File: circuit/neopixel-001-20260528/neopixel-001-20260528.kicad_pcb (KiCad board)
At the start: 2 copper layers, 114.3 x 114.3 mm, 67 parts, among them J1 Conn_NeoPixel, J2 Conn_01x02_Pin, J3 Conn_01x02_Pin, P1 ESP32C3_{1}, P10 unitV3, P11 unitV4, P12 unitV4, P2 ESP32C3_{1}, P3 ESP32C3_{2}, P4 ESP32C3_{2}, P5 unitV1, P6 unitV1, P7 unitV2, P8 unitV2, P9 unitV3, SW1 SW_SPST_LED, SW2 SW_SPST_LED, SW3 SW_SPST_LED, SW4 SW_SPST_LED, U1 SSD1306, U2 Aexit_0-50_Voltmeter

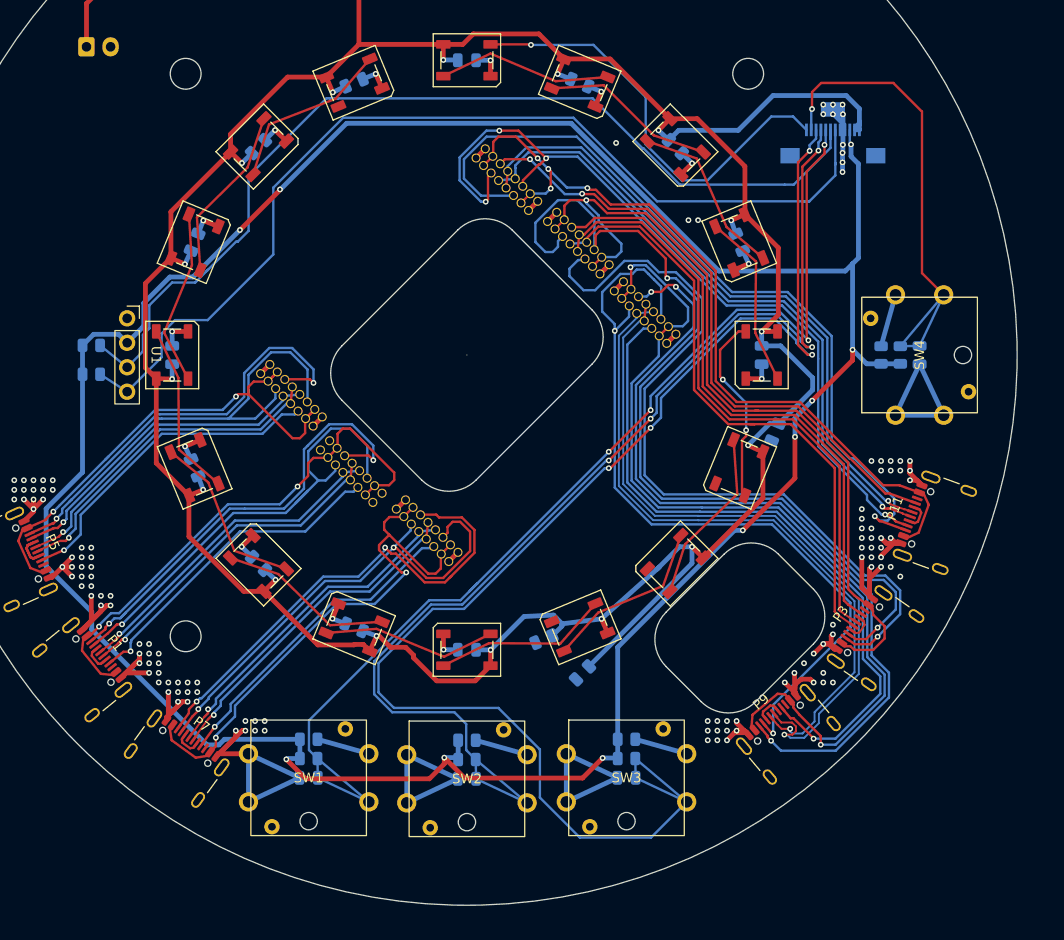
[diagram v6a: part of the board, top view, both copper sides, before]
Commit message: Update ネオピクセル基板のPCBを進めた。タクトスイッチだけ怪しい
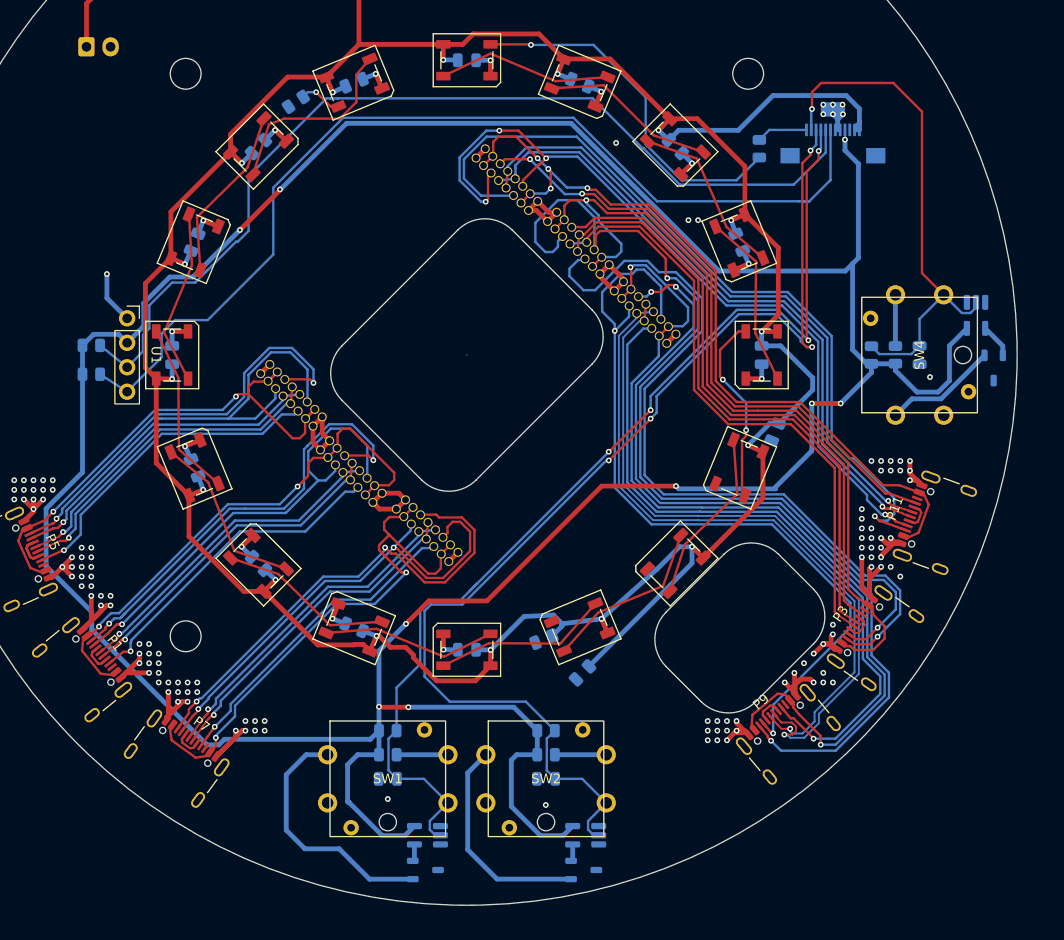
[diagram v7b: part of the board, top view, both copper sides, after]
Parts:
- removed C20: 100n, Capacitor_SMD:C_0805_2012Metric
- removed SW3: SW_SPST_LED, @Thrive_footprint_neopixel:ST-12-401FC-G
- added Q1: NMOS, Package_TO_SOT_SMD:TSOT-23, B.Cu at (-4.31, 53.5)
- added Q2: NMOS, Package_TO_SOT_SMD:TSOT-23, B.Cu at (12.1, 53.5)
- added Q3: NMOS, Package_TO_SOT_SMD:TSOT-23, B.Cu at (54.7, 1.34)
- added U3: 74AHC1G04, Package_TO_SOT_SMD:SOT-23-5_HandSoldering, B.Cu at (-4.10, 49.9)
- added U4: 74AHC1G04, Package_TO_SOT_SMD:SOT-23-5_HandSoldering, B.Cu at (12.3, 49.9)
- added U5: 74AHC1G04, Package_TO_SOT_SMD:SOT-23-5_HandSoldering, B.Cu at (52.9, -4.12)
- R10: value 330 -> 500
- R9: value 10k -> 500
- moved R10 66.2 mm to (-17.8, -26.3), turned to -146.25 degrees
- moved C19 53.4 mm to (47.0, 0.00), turned to 90 degrees
- moved R7 49.0 mm to (42.0, 0.00), turned to -90 degrees
- moved R8 48.7 mm to (44.5, -0.02), turned to -90 degrees
- moved R9 25.9 mm to (30.4, -21.4)
- moved R5 8.75 mm to (8.22, 39.0)
- moved R3 8.71 mm to (-8.22, 39.0)
- moved R4 8.37 mm to (-8.22, 41.5)
- moved R6 8.35 mm to (8.22, 41.5)
- moved C17 8.22 mm to (-8.22, 44.0)
- moved SW1 8.22 mm to (-8.22, 44.0)
- moved C18 8.22 mm to (8.22, 44.0)
- moved SW2 8.22 mm to (8.22, 44.0)
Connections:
- C19 pad 2: SW_{TCT3} -> SW_{START}
- D1 pad 4: SIG_{NeoPixel} -> Net-(D1-DIN)
- D16 pad 2: unconnected-(D16-DOUT-Pad2) -> Net-(D16-DOUT)
- J1 pad 10: SW_{TCT3} -> SW_{TCT2}
- J1 pad 3: +3.3V -> +5V
- J1 pad 4: GND -> +3.3V
- J1 pad 6: SDA -> GND
- J1 pad 7: SCL -> SDA
- J1 pad 8: SW_{TCT1} -> SCL
- J1 pad 9: SW_{TCT2} -> SW_{TCT1}
- R10 pad 1: Net-(SW4-A) -> Net-(D16-DOUT)
- R10 pad 2: +3.3V -> GND
- R7 pad 1: SW_{TCT3} -> SW_{START}
- R8 pad 1: Net-(SW3-A) -> Net-(SW4-A)
- R9 pad 1: SW_{START} -> SIG_{NeoPixel}
- R9 pad 2: +3.3V -> Net-(D1-DIN)
- SW1 pad 3: GND -> Net-(Q1-D)
- SW2 pad 3: GND -> Net-(Q2-D)
- SW4 pad 3: GND -> Net-(Q3-D)
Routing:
- net SW_{TCT3}: track 148.8 -> 0.00 mm, vias 4 -> 0
- net +3.3V: track 285.5 -> 339.6 mm, vias 10 -> 9
- net GND: track 235.8 -> 189.3 mm
- net SIG_{NeoPixel}: track 44.8 -> 5.32 mm, vias 1 -> 0
- net Net-(D1-DIN): track 0.00 -> 37.6 mm, vias 0 -> 1
- net Net-(Q1-D): track 0.00 -> 26.2 mm
- net Net-(Q2-D): track 0.00 -> 22.6 mm
- net Net-(Q3-D): track 0.00 -> 11.8 mm
- net Net-(SW3-A): track 5.54 -> 0.00 mm
- net Net-(D16-DOUT): track 0.00 -> 4.47 mm, vias 0 -> 1
- net SW_{TCT1}: track 114.8 -> 110.6 mm
- net Net-(Q3-G): track 0.00 -> 3.55 mm
- net SW_{START}: track 51.8 -> 53.9 mm
- net Net-(D15-DOUT): track 18.3 -> 20.3 mm
- net P1_CC: track 49.6 -> 47.8 mm
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
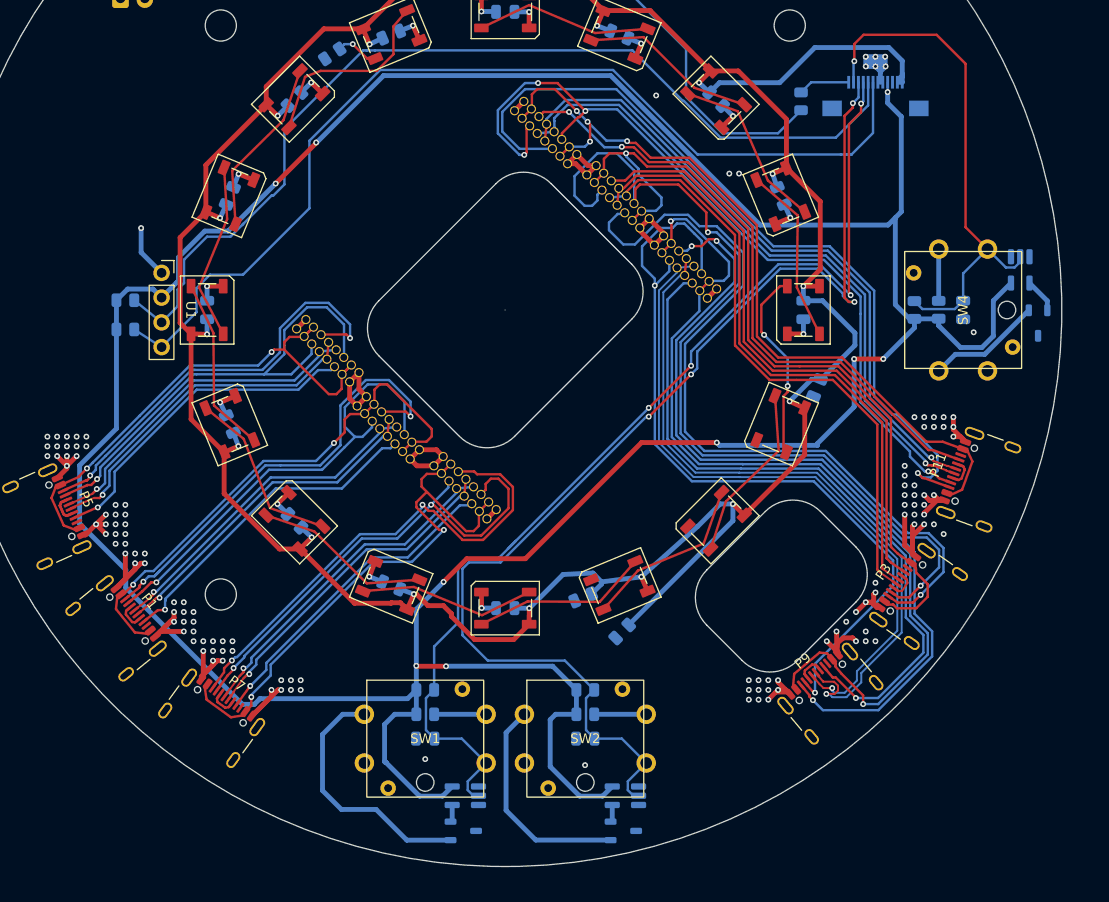
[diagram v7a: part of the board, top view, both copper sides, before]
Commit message: Update ネオピクセル基板のSW周りを更新。DRおなしゃあす
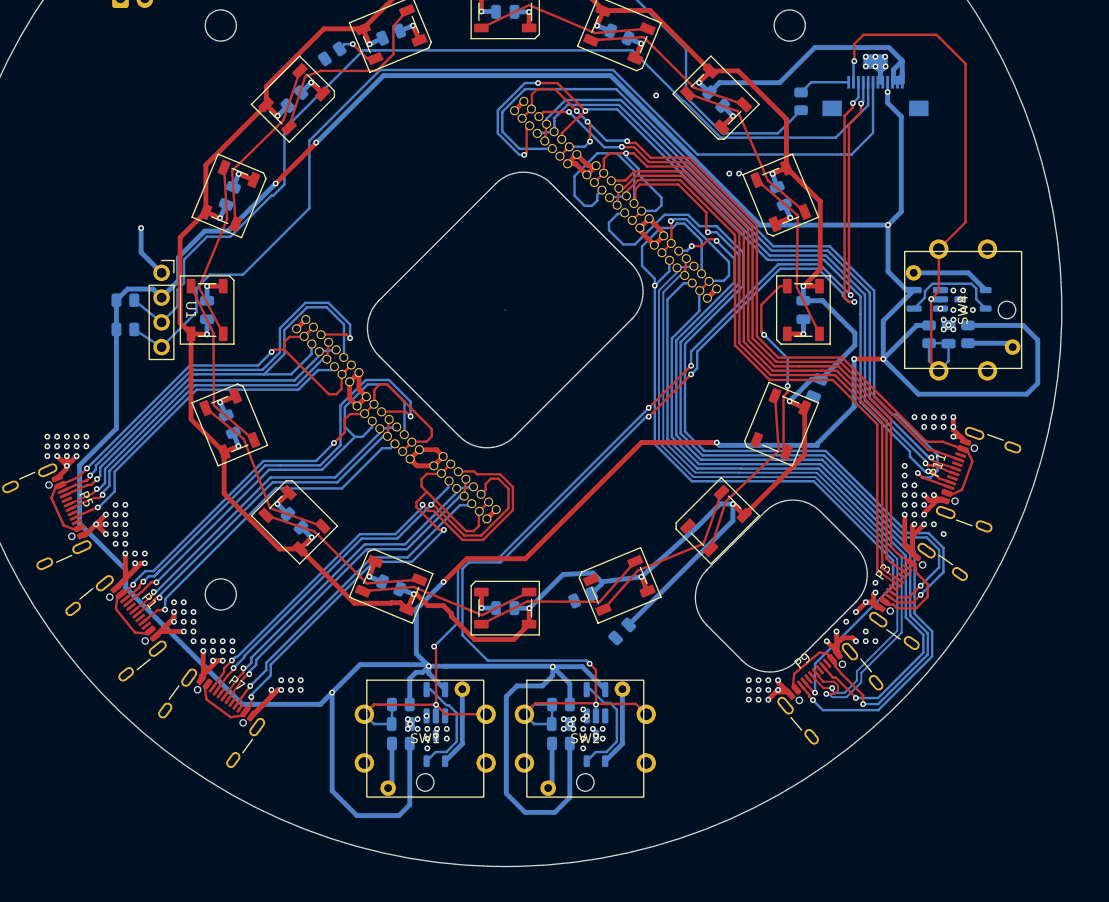
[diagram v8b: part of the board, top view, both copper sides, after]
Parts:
- moved U3 10.0 mm to (-7.12, 40.3), turned to 90 degrees
- moved U4 10.0 mm to (9.31, 40.3), turned to 90 degrees
- moved U5 10.0 mm to (43.3, -1.09), turned to 180 degrees
- moved Q1 8.92 mm to (-7.12, 45.0), turned to 90 degrees
- moved Q2 8.92 mm to (9.31, 45.0), turned to 90 degrees
- moved Q3 7.12 mm to (48.0, -1.09), turned to 180 degrees
- moved R8 3.93 mm to (47.5, 2.50), turned to 90 degrees
- moved R4 3.91 mm to (-10.7, 44.5), turned to 0 degrees
- moved R6 3.91 mm to (5.72, 44.5), turned to 0 degrees
- moved C18 2.92 mm to (5.72, 42.5), turned to 180 degrees
- moved R5 2.92 mm to (5.72, 40.5), turned to 0 degrees
- moved C17 2.92 mm to (-10.7, 42.5), turned to 180 degrees
- moved C19 2.92 mm to (45.5, 2.50), turned to -90 degrees
- moved R3 2.92 mm to (-10.7, 40.5), turned to 0 degrees
- moved R7 2.92 mm to (43.5, 2.50), turned to 90 degrees
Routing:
- net +3.3V: track 339.6 -> 392.8 mm, vias 9 -> 11
- net (no net): track 21.0 -> 0.00 mm
- net Net-(Q1-D): track 26.2 -> 8.12 mm
- net Net-(Q2-D): track 22.6 -> 8.12 mm
- net Net-(Q2-G): track 1.78 -> 11.1 mm
- net Net-(Q1-G): track 1.78 -> 10.9 mm
- net SW_{TCT2}: track 119.1 -> 128.2 mm, vias 4 -> 6
- net Net-(Q3-G): track 3.55 -> 10.5 mm
- net SW_{START}: track 53.9 -> 59.8 mm, vias 1 -> 2
- net SW_{TCT1}: track 110.6 -> 116.1 mm, vias 4 -> 6
- net Net-(Q3-D): track 11.8 -> 8.12 mm
- net +5V: track 334.6 -> 337.7 mm
- net Net-(SW2-A): track 5.34 -> 4.74 mm
- net Net-(SW1-A): track 5.34 -> 4.74 mm
- net Net-(SW4-A): track 5.32 -> 4.74 mm
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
